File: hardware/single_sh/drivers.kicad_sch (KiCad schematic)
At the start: 64 parts, among them U1 AT8833CQ, U10 AT8833CQ, U2 AT8833CQ, U3 AT8833CQ, U4 AT8833CQ, U5 AT8833CQ, U6 AT8833CQ, U7 AT8833CQ, U8 AT8833CQ, U9 AT8833CQ

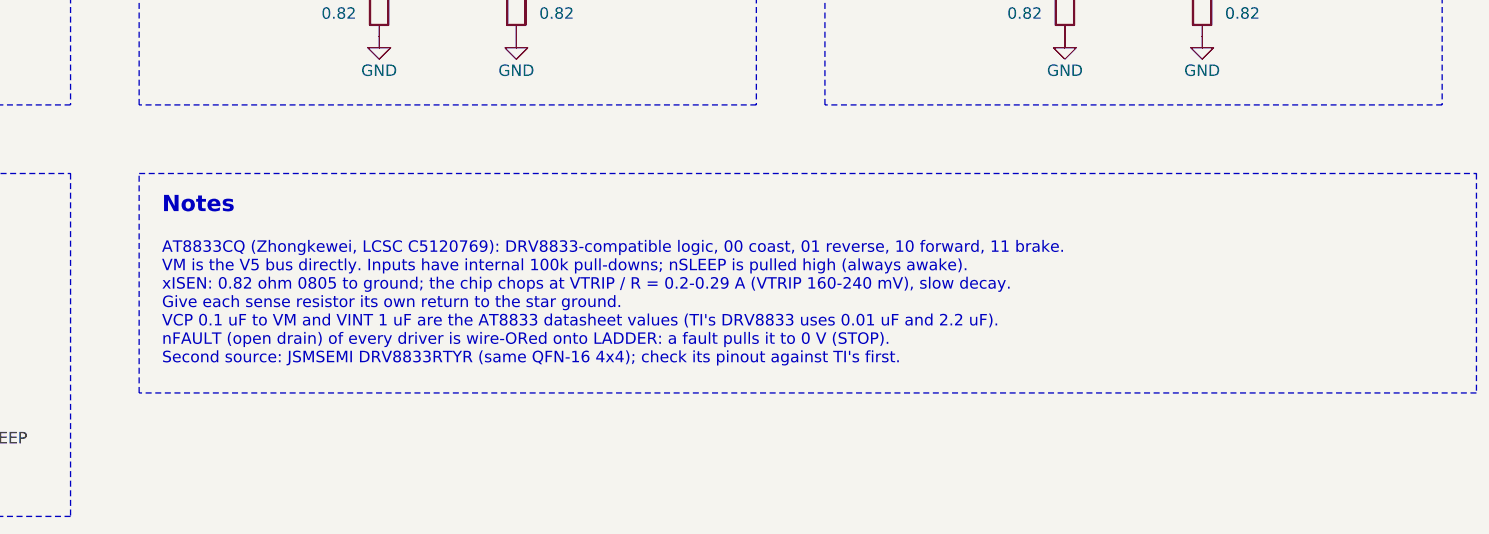
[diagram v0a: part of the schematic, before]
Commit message: single_sh: 0603 sense resistors; refilled zones, fab output
Sense resistors move from 0805 to 0603 (Viking SR731JTTDR820F, C186570,
250 mW); holding a coil at the current-limit trip is now 28 % of rating.
Swapped in place on the routed board: ISEN pad kept, GND pad 0.275 mm
inboard (R5/R11 keep the GND pad instead). Zones refilled after the route
cleanup and trace edits. DRC: 0 unconnected, 0 parity, no copper
violations; 4 silkscreen warnings.

Schematics, BOMs, generators and README updated; JLCPCB Gerbers/BOM/CPL
regenerated and placement-checked.

Co-Authored-By: Claude Opus 5.5 <noreply@anthropic.com>
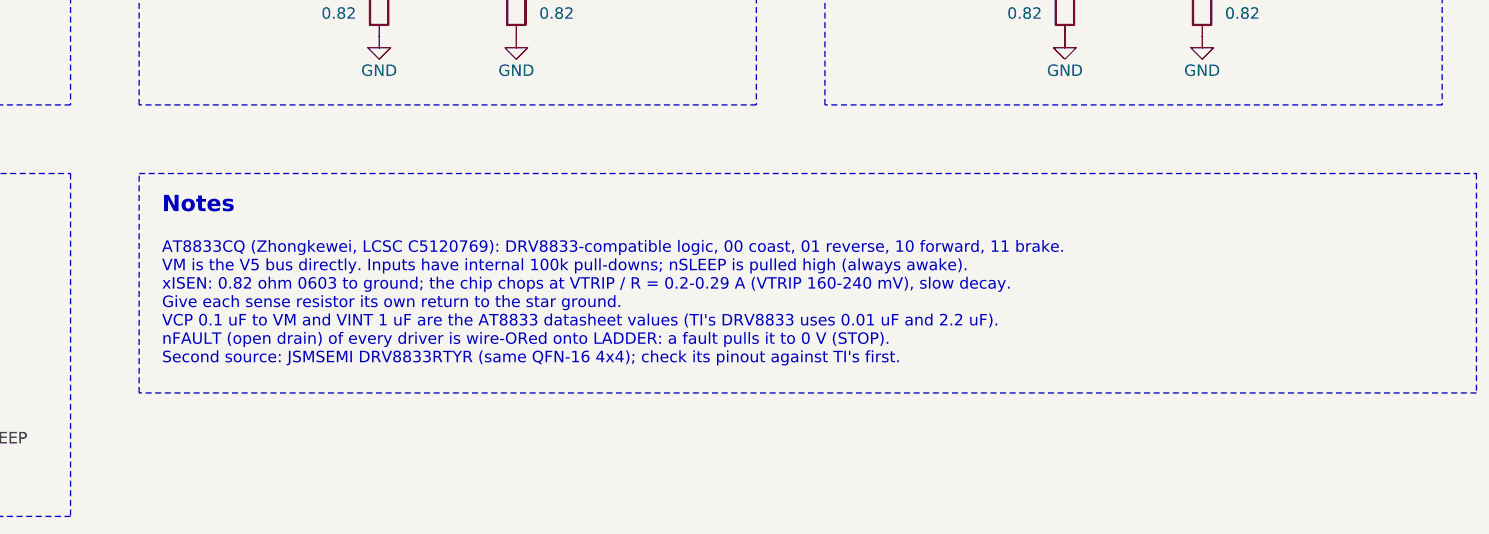
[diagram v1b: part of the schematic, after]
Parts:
- R1, R10, R11, R12, R13, R14, R15, R16, R17, R18, R19, R2, R20, R3, R4, R5, R6, R7, R8, R9: footprint Resistor_SMD:R_0805_2012Metric -> Resistor_SMD:R_0603_1608Metric; LCSC C513694 -> C186570; MPN RL0805FR-070R82L -> SR731JTTDR820F
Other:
- note added: "AT8833CQ (Zhongkewei, LCSC C5120769): DRV8833-compatible logic, 00 coast, 01 reverse, 10 forward, 11 brake. VM is the V5 bus directly. Inputs have internal 100k pull-downs; nSLEEP is pulled high (always awake). xISEN: 0.82 ohm 0603 to ground; the chip chops at VTRIP / R = 0.2-0.29 A (VTRIP 160-240 mV), slow decay. Give each sense resistor its own return to the star ground. VCP 0.1 uF to VM and VI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"
- note removed: "AT8833CQ (Zhongkewei, LCSC C5120769): DRV8833-compatible logic, 00 coast, 01 reverse, 10 forward, 11 brake. VM is the V5 bus directly. Inputs have internal 100k pull-downs; nSLEEP is pulled high (always awake). xISEN: 0.82 ohm 0805 to ground; the chip chops at VTRIP / R = 0.2-0.29 A (VTRIP 160-240 mV), slow decay. Give each sense resistor its own return to the star ground. VCP 0.1 uF to VM and VI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"
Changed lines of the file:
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@@
 			)
 		)
-		(property "Footprint" "Resistor_SMD:R_0805_2012Metric"
+		(property "Footprint" "Resistor_SMD:R_0603_1608Metric"
 			(at 43.18 90.17 0)
 			(hide yes)
@@
 			)
 		)
-		(property "LCSC" "C513694"
+		(property "LCSC" "C186570"
 			(at 43.18 90.17 0)
 			(hide yes)
@@
 			)
 		)
-		(property "MPN" "RL0805FR-070R82L"
+		(property "MPN" "SR731JTTDR820F"
 			(at 43.18 90.17 0)
 			(hide yes)
@@
 			)
 		)
-		(property "Footprint" "Resistor_SMD:R_0805_2012Metric"
+		(property "Footprint" "Resistor_SMD:R_0603_1608Metric"
 			(at 58.42 90.17 0)
 			(hide yes)
@@
 			)
 		)
-		(property "LCSC" "C513694"
+		(property "LCSC" "C186570"
 			(at 58.42 90.17 0)
 			(hide yes)
@@
 			)
 		)
-		(property "MPN" "RL0805FR-070R82L"
+		(property "MPN" "SR731JTTDR820F"
 			(at 58.42 90.17 0)
 			(hide yes)
@@
 			)
 		)
-		(property "Footprint" "Resistor_SMD:R_0805_2012Metric"
+		(property "Footprint" "Resistor_SMD:R_0603_1608Metric"
 			(at 119.38 90.17 0)
 			(hide yes)
@@
 			)
 		)
-		(property "LCSC" "C513694"
+		(property "LCSC" "C186570"
 			(at 119.38 90.17 0)
 			(hide yes)
@@
 			)
 		)
-		(property "MPN" "RL0805FR-070R82L"
+		(property "MPN" "SR731JTTDR820F"
 			(at 119.38 90.17 0)
 			(hide yes)
@@
 			)
 		)
-		(property "Footprint" "Resistor_SMD:R_0805_2012Metric"
+		(property "Footprint" "Resistor_SMD:R_0603_1608Metric"
 			(at 134.62 90.17 0)
 			(hide yes)
@@
 			)
 		)
-		(property "LCSC" "C513694"
+		(property "LCSC" "C186570"
 			(at 134.62 90.17 0)
 			(hide yes)
@@
 			)
 		)
-		(property "MPN" "RL0805FR-070R82L"
+		(property "MPN" "SR731JTTDR820F"
 			(at 134.62 90.17 0)
 			(hide yes)
@@
 			)
 		)
-		(property "Footprint" "Resistor_SMD:R_0805_2012Metric"
+		(property "Footprint" "Resistor_SMD:R_0603_1608Metric"
 			(at 195.58 90.17 0)
 			(hide yes)
@@
 			)
 		)
-		(property "LCSC" "C513694"
+		(property "LCSC" "C186570"
 			(at 195.58 90.17 0)
 			(hide yes)
@@
 			)
 		)
-		(property "MPN" "RL0805FR-070R82L"
+		(property "MPN" "SR731JTTDR820F"
 			(at 195.58 90.17 0)
 			(hide yes)
@@
 			)
 		)
-		(property "Footprint" "Resistor_SMD:R_0805_2012Metric"
+		(property "Footprint" "Resistor_SMD:R_0603_1608Metric"
 			(at 210.82 90.17 0)
 			(hide yes)
@@
 			)
 		)
-		(property "LCSC" "C513694"
+		(property "LCSC" "C186570"
 			(at 210.82 90.17 0)
 			(hide yes)
@@
 			)
 		)
-		(property "MPN" "RL0805FR-070R82L"
+		(property "MPN" "SR731JTTDR820F"
 			(at 210.82 90.17 0)
 			(hide yes)
@@
 			)
 		)
-		(property "Footprint" "Resistor_SMD:R_0805_2012Metric"
+		(property "Footprint" "Resistor_SMD:R_0603_1608Metric"
 			(at 271.78 90.17 0)
 			(hide yes)
@@
 			)
 		)
-		(property "LCSC" "C513694"
+		(property "LCSC" "C186570"
 			(at 271.78 90.17 0)
 			(hide yes)
@@
 			)
 		)
-		(property "MPN" "RL0805FR-070R82L"
+		(property "MPN" "SR731JTTDR820F"
 			(at 271.78 90.17 0)
 			(hide yes)
@@
 			)
 		)
-		(property "Footprint" "Resistor_SMD:R_0805_2012Metric"
+		(property "Footprint" "Resistor_SMD:R_0603_1608Metric"
 			(at 287.02 90.17 0)
 			(hide yes)
@@
 			)
 		)
-		(property "LCSC" "C513694"
+		(property "LCSC" "C186570"
 			(at 287.02 90.17 0)
 			(hide yes)
@@
 			)
 		)
-		(property "MPN" "RL0805FR-070R82L"
+		(property "MPN" "SR731JTTDR820F"
 			(at 287.02 90.17 0)
 			(hide yes)
@@
 			)
 		)
-		(property "Footprint" "Resistor_SMD:R_0805_2012Metric"
+		(property "Footprint" "Resistor_SMD:R_0603_1608Metric"
 			(at 347.98 90.17 0)
 			(hide yes)
@@
 			)
 		)
-		(property "LCSC" "C513694"
+		(property "LCSC" "C186570"
 			(at 347.98 90.17 0)
 			(hide yes)
@@
 			)
 		)
-		(property "MPN" "RL0805FR-070R82L"
+		(property "MPN" "SR731JTTDR820F"
 			(at 347.98 90.17 0)
 			(hide yes)
@@
 			)
 		)
-		(property "Footprint" "Resistor_SMD:R_0805_2012Metric"
+		(property "Footprint" "Resistor_SMD:R_0603_1608Metric"
 			(at 363.22 90.17 0)
 			(hide yes)
@@
 			)
 		)
-		(property "LCSC" "C513694"
+		(property "LCSC" "C186570"
 			(at 363.22 90.17 0)
 			(hide yes)
@@
 			)
 		)
-		(property "MPN" "RL0805FR-070R82L"
+		(property "MPN" "SR731JTTDR820F"
 			(at 363.22 90.17 0)
 			(hide yes)
@@
 			)
 		)
-		(property "Footprint" "Resistor_SMD:R_0805_2012Metric"
+		(property "Footprint" "Resistor_SMD:R_0603_1608Metric"
 			(at 43.18 176.53 0)
 			(hide yes)
@@
 			)
 		)
-		(property "LCSC" "C513694"
+		(property "LCSC" "C186570"
 			(at 43.18 176.53 0)
 			(hide yes)
@@
 			)
 		)
-		(property "MPN" "RL0805FR-070R82L"
+		(property "MPN" "SR731JTTDR820F"
 			(at 43.18 176.53 0)
 			(hide yes)
@@
 			)
 		)
-		(property "Footprint" "Resistor_SMD:R_0805_2012Metric"
+		(property "Footprint" "Resistor_SMD:R_0603_1608Metric"
 			(at 58.42 176.53 0)
 			(hide yes)
@@
 			)
 		)
-		(property "LCSC" "C513694"
+		(property "LCSC" "C186570"
 			(at 58.42 176.53 0)
 			(hide yes)
@@
 			)
 		)
-		(property "MPN" "RL0805FR-070R82L"
+		(property "MPN" "SR731JTTDR820F"
 			(at 58.42 176.53 0)
 			(hide yes)
@@
 			)
 		)
-		(property "Footprint" "Resistor_SMD:R_0805_2012Metric"
+		(property "Footprint" "Resistor_SMD:R_0603_1608Metric"
 			(at 119.38 176.53 0)
 			(hide yes)
@@
 			)
 		)
-		(property "LCSC" "C513694"
+		(property "LCSC" "C186570"
 			(at 119.38 176.53 0)
 			(hide yes)
@@
 			)
 		)
-		(property "MPN" "RL0805FR-070R82L"
+		(property "MPN" "SR731JTTDR820F"
 			(at 119.38 176.53 0)
 			(hide yes)
@@
 			)
 		)
-		(property "Footprint" "Resistor_SMD:R_0805_2012Metric"
+		(property "Footprint" "Resistor_SMD:R_0603_1608Metric"
 			(at 134.62 176.53 0)
 			(hide yes)
@@
 			)
 		)
-		(property "LCSC" "C513694"
+		(property "LCSC" "C186570"
 			(at 134.62 176.53 0)
 			(hide yes)
@@
 			)
 		)
-		(property "MPN" "RL0805FR-070R82L"
+		(property "MPN" "SR731JTTDR820F"
 			(at 134.62 176.53 0)
 			(hide yes)
@@
 			)
 		)
-		(property "Footprint" "Resistor_SMD:R_0805_2012Metric"
+		(property "Footprint" "Resistor_SMD:R_0603_1608Metric"
 			(at 195.58 176.53 0)
 			(hide yes)
@@
 			)
 		)
-		(property "LCSC" "C513694"
+		(property "LCSC" "C186570"
 			(at 195.58 176.53 0)
 			(hide yes)
@@
 			)
 		)
-		(property "MPN" "RL0805FR-070R82L"
+		(property "MPN" "SR731JTTDR820F"
 			(at 195.58 176.53 0)
 			(hide yes)
@@
 			)
 		)
-		(property "Footprint" "Resistor_SMD:R_0805_2012Metric"
+		(property "Footprint" "Resistor_SMD:R_0603_1608Metric"
 			(at 210.82 176.53 0)
 			(hide yes)
@@
 			)
 		)
-		(property "LCSC" "C513694"
+		(property "LCSC" "C186570"
 			(at 210.82 176.53 0)
 			(hide yes)
@@
 			)
 		)
-		(property "MPN" "RL0805FR-070R82L"
+		(property "MPN" "SR731JTTDR820F"
 			(at 210.82 176.53 0)
 			(hide yes)
@@
 			)
 		)
-		(property "Footprint" "Resistor_SMD:R_0805_2012Metric"
+		(property "Footprint" "Resistor_SMD:R_0603_1608Metric"
 			(at 271.78 176.53 0)
 			(hide yes)
@@
 			)
 		)
-		(property "LCSC" "C513694"
+		(property "LCSC" "C186570"
 			(at 271.78 176.53 0)
 			(hide yes)
@@
 			)
 		)
-		(property "MPN" "RL0805FR-070R82L"
+		(property "MPN" "SR731JTTDR820F"
 			(at 271.78 176.53 0)
 			(hide yes)
@@
 			)
 		)
-		(property "Footprint" "Resistor_SMD:R_0805_2012Metric"
+		(property "Footprint" "Resistor_SMD:R_0603_1608Metric"
 			(at 287.02 176.53 0)
 			(hide yes)
@@
 			)
 		)
-		(property "LCSC" "C513694"
+		(property "LCSC" "C186570"
 			(at 287.02 176.53 0)
 			(hide yes)
@@
 			)
 		)
-		(property "MPN" "RL0805FR-070R82L"
+		(property "MPN" "SR731JTTDR820F"
 			(at 287.02 176.53 0)
 			(hide yes)
@@
 			)
 		)
-		(property "Footprint" "Resistor_SMD:R_0805_2012Metric"
+		(property "Footprint" "Resistor_SMD:R_0603_1608Metric"
 			(at 347.98 176.53 0)
 			(hide yes)
@@
 			)
 		)
-		(property "LCSC" "C513694"
+		(property "LCSC" "C186570"
 			(at 347.98 176.53 0)
 			(hide yes)
@@
 			)
 		)
-		(property "MPN" "RL0805FR-070R82L"
+		(property "MPN" "SR731JTTDR820F"
 			(at 347.98 176.53 0)
 			(hide yes)
@@
 			)
 		)
-		(property "Footprint" "Resistor_SMD:R_0805_2012Metric"
+		(property "Footprint" "Resistor_SMD:R_0603_1608Metric"
 			(at 363.22 176.53 0)
 			(hide yes)
@@
 			)
 		)
-		(property "LCSC" "C513694"
+		(property "LCSC" "C186570"
 			(at 363.22 176.53 0)
 			(hide yes)
@@
 			)
 		)
-		(property "MPN" "RL0805FR-070R82L"
+		(property "MPN" "SR731JTTDR820F"
 			(at 363.22 176.53 0)
 			(hide yes)
@@
 		)
 	)
-	(text "AT8833CQ (Zhongkewei, LCSC C5120769): DRV8833-compatible logic, 00 coast, 01 reverse, 10 forward, 11 brake.\nVM is the V5 bus directly. Inputs have internal 100k pull-downs; nSLEEP is pulled high (always awake).\nxISEN: 0.82 ohm 0805 to ground; the chip chops at VTRIP / R = 0.2-0.29 A (VTRIP 160-240 mV), slow decay.\nGive each sense resistor its own return to the star ground.\nVCP 0.1 uF to VM and VINT 1 uF are the AT8833 datasheet values (TI's DRV8833 uses 0.01 uF and 2.2 uF).\nnFAULT (open drain) of every driver is wire-ORed onto LADDER: a fault pulls it to 0 V (STOP).\nSecond source: JSMSEMI DRV8833RTYR (same QFN-16 4x4); check its pinout against TI's first."
+	(text "AT8833CQ (Zhongkewei, LCSC C5120769): DRV8833-compatible logic, 00 coast, 01 reverse, 10 forward, 11 brake.\nVM is the V5 bus directly. Inputs have internal 100k pull-downs; nSLEEP is pulled high (always awake).\nxISEN: 0.82 ohm 0603 to ground; the chip chops at VTRIP / R = 0.2-0.29 A (VTRIP 160-240 mV), slow decay.\nGive each sense resistor its own return to the star ground.\nVCP 0.1 uF to VM and VINT 1 uF are the AT8833 datasheet values (TI's DRV8833 uses 0.01 uF and 2.2 uF).\nnFAULT (open drain) of every driver is wire-ORed onto LADDER: a fault pulls it to 0 V (STOP).\nSecond source: JSMSEMI DRV8833RTYR (same QFN-16 4x4); check its pinout against TI's first."
 		(exclude_from_sim no)
 		(at 95.25 203.2 0)

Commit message: single_sh_proto: all-0603 basic-parts prototype board, as ordered
150 x 30 mm 4-layer board, fully routed (0.52/0.3 vias, 45-degree traces,
centred pad entries, no vias in pads), JLCDFM clean. Corrected nested
dual-motor connector pinout, bring-up test points, back-silk squid art.
L1 substituted (C411344); status LED D2 is the 5050 WS2812B (C2843785),
left off the Economic PCBA order for hand soldering.

Generator updates for the proto board (build.py, pcbgen.py, jlcfab.py,
single_sh_sch.py, add_testpoints.py, squid_silk.py) and regenerated
outputs for the other boards.

Ordered from JLCPCB 2026-10-11: 5 boards, Economic PCBA.

Co-Authored-By: Claude Opus 5.5 <noreply@anthropic.com>
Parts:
- R1, R10, R11, R12, R13, R14, R15, R16, R17, R18, R19, R2, R20, R3, R4, R5, R6, R7, R8, R9: value 0.82 -> 1; LCSC C186570 -> C22936; MPN SR731JTTDR820F -> 0603WAF100KT5E; Note chops at 0.2-0.29 A (VTRIP 160-240 mV); Kelvin return -> chops at 0.16-0.24 A (VTRIP 160-240 mV); Kelvin return
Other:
- note added: "AT8833CQ (Zhongkewei, LCSC C5120769): DRV8833-compatible logic, 00 coast, 01 reverse, 10 forward, 11 brake. VM is the V5 bus directly. Inputs have internal 100k pull-downs; nSLEEP is pulled high (always awake). xISEN: 1 ohm 0603 to ground; the chip chops at VTRIP / R = 0.16-0.24 A (VTRIP 160-240 mV), slow decay. Give each sense resistor its own return to the star ground. VCP 0.1 uF to VM and VINT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"
- note removed: "AT8833CQ (Zhongkewei, LCSC C5120769): DRV8833-compatible logic, 00 coast, 01 reverse, 10 forward, 11 brake. VM is the V5 bus directly. Inputs have internal 100k pull-downs; nSLEEP is pulled high (always awake). xISEN: 0.82 ohm 0603 to ground; the chip chops at VTRIP / R = 0.2-0.29 A (VTRIP 160-240 mV), slow decay. Give each sense resistor its own return to the star ground. VCP 0.1 uF to VM and VI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"
